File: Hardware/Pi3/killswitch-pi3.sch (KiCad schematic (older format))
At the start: 32 parts, among them J1 PWR_IN, J2 REMOTE, J3 PI, J4 Conn_01x02, J5 Conn_01x02, Q1 Q_PMOS_GSD, SW1 SW_Push, U1 ATTINY84-20SSU, U2 TSDP341xx, U3 AZ1117-3.3, U4 TXB0108DQSR

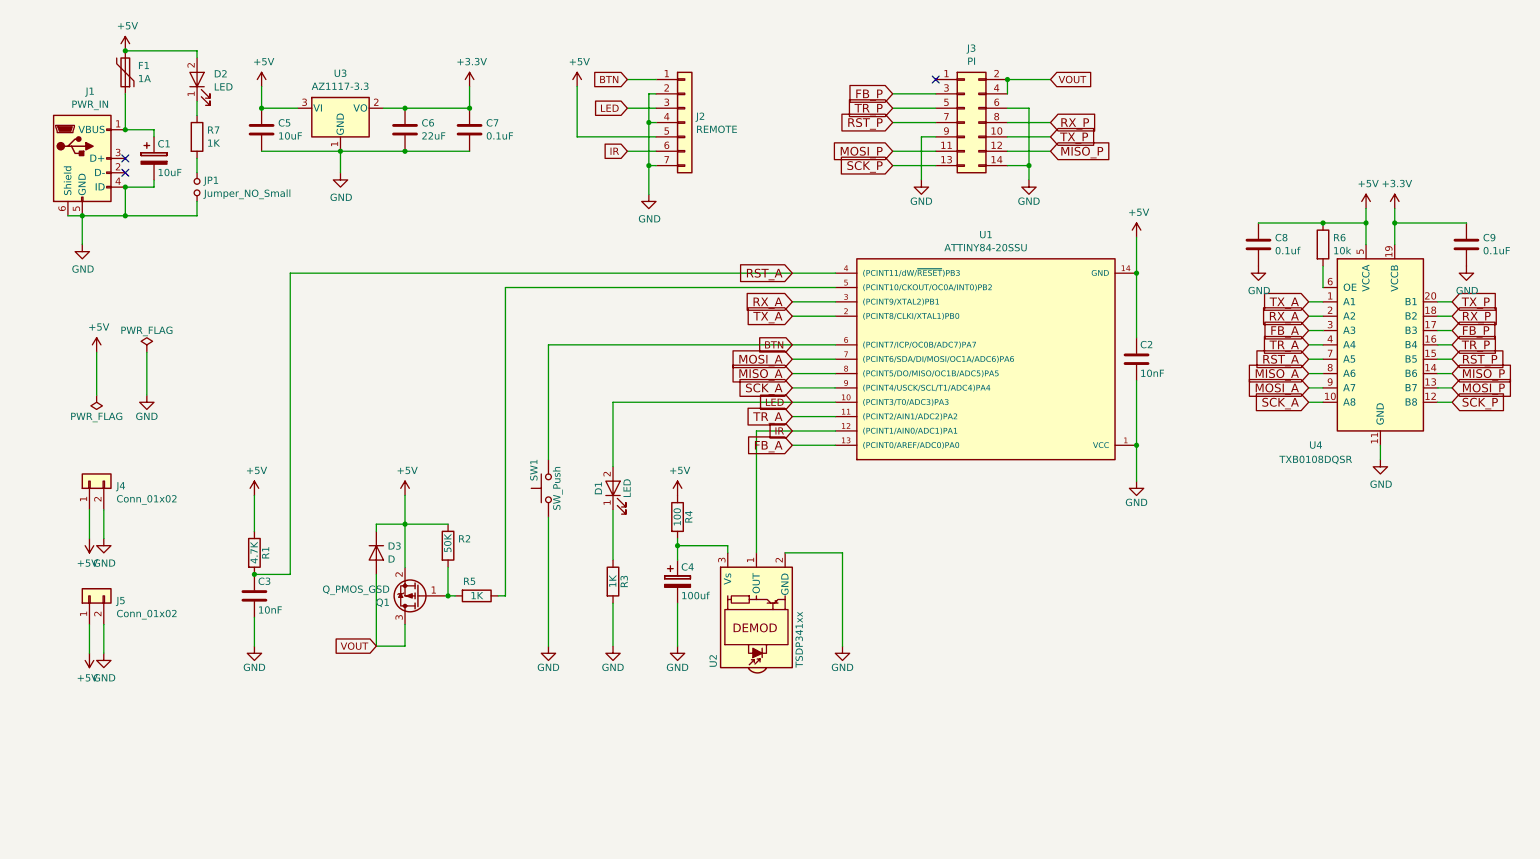
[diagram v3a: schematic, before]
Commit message: Clean up schematic/remove level shifter
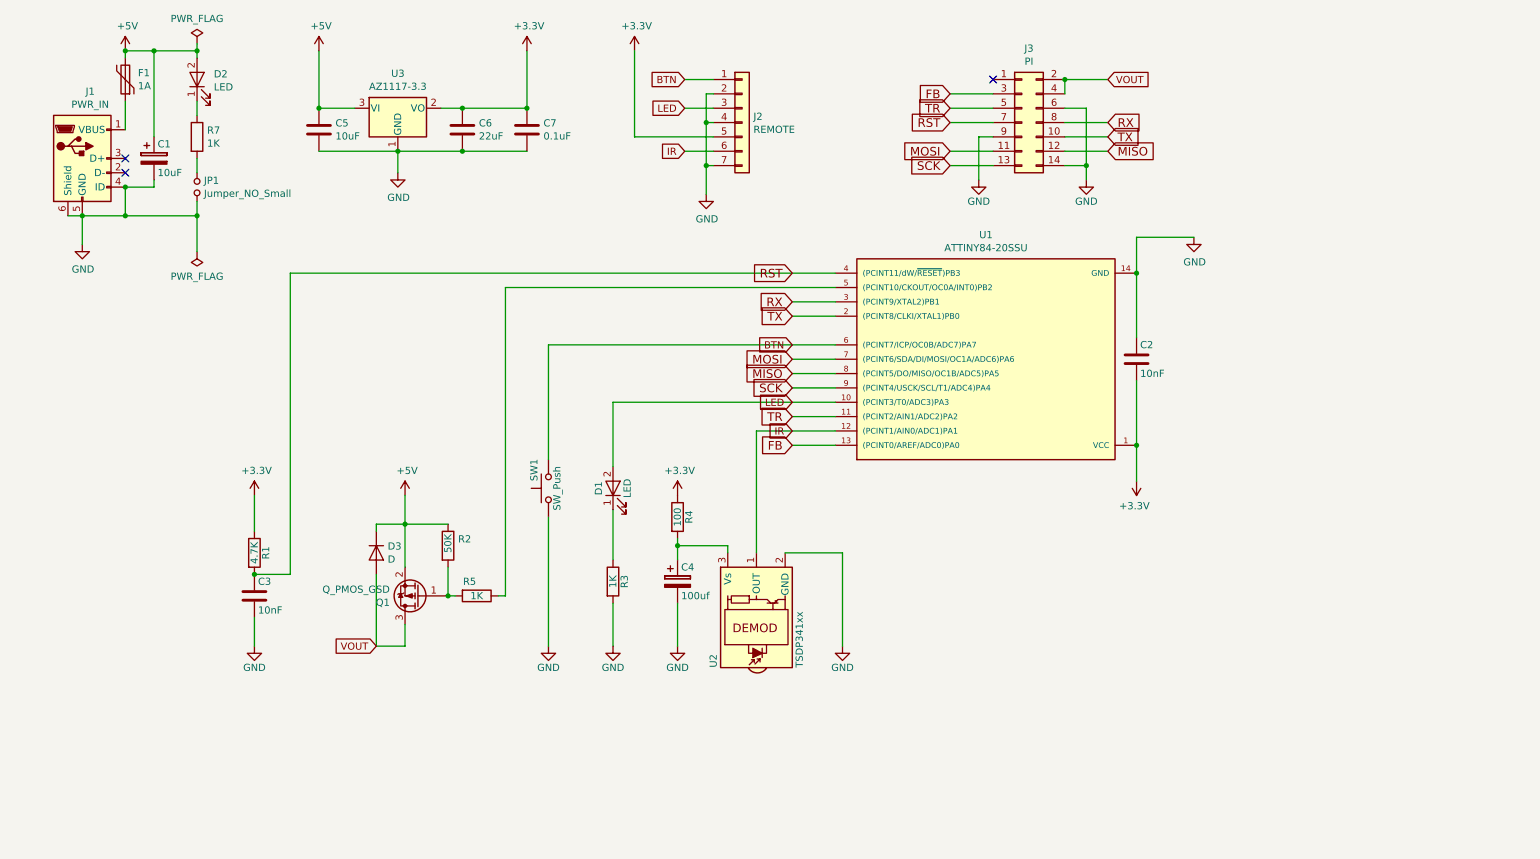
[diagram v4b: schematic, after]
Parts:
- removed C8: 0.1uf, Capacitors_SMD:C_0603_HandSoldering, symbol device:C
- removed C9: 0.1uF, Capacitors_SMD:C_0603_HandSoldering, symbol device:C
- removed J4: Conn_01x02, Connectors_JST:JST_XH_B02B-XH-A_02x2.50mm_Straight, symbol conn:Conn_01x02
- removed J5: Conn_01x02, Pin_Headers:Pin_Header_Straight_1x02_Pitch2.54mm, symbol conn:Conn_01x02
- removed R6: 10k, Resistors_SMD:R_0603_HandSoldering, symbol device:R
- removed U4: TXB0108DQSR, Housings_SON:USON-20_2x4mm_Pitch0.4mm, symbol texas:TXB0108DQSR
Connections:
- net FB_P is gone; now on net FB: J3.3 (Pin_3)
- net MISO_P is gone; now on net MISO: J3.12 (Pin_12)
- net MOSI_P is gone; now on net MOSI: J3.11 (Pin_11)
- net RST_P is gone; now on net RST: J3.7 (Pin_7)
- net RX_P is gone; now on net RX: J3.8 (Pin_8)
- net SCK_P is gone; now on net SCK: J3.13 (Pin_13)
- net TR_P is gone; now on net TR: J3.5 (Pin_5)
- net TX_P is gone; now on net TX: J3.10 (Pin_10)
- net +3V3: now also C2.2, J2.5 (Pin_5), R1.1, R4.1, U1.1 (VCC)
- net +5V: now also C1.1; no longer C2.1, J2.5 (Pin_5), R1.1, R4.1, U1.14 (GND)
- net GND: now also C2.1, U1.14 (GND); no longer C2.2, U1.1 (VCC)
- net at F1.1, J1.1 (VBUS): no longer C1.1
- net FB_A renamed FB
- net MISO_A renamed MISO
- net MOSI_A renamed MOSI
- net RST_A renamed RST
- net RX_A renamed RX
- net SCK_A renamed SCK
- net TR_A renamed TR
- net TX_A renamed TX
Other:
- moved on the sheet: C5, C6, C7, F1, J2, J3, U3

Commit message: changed to ATTiny1634
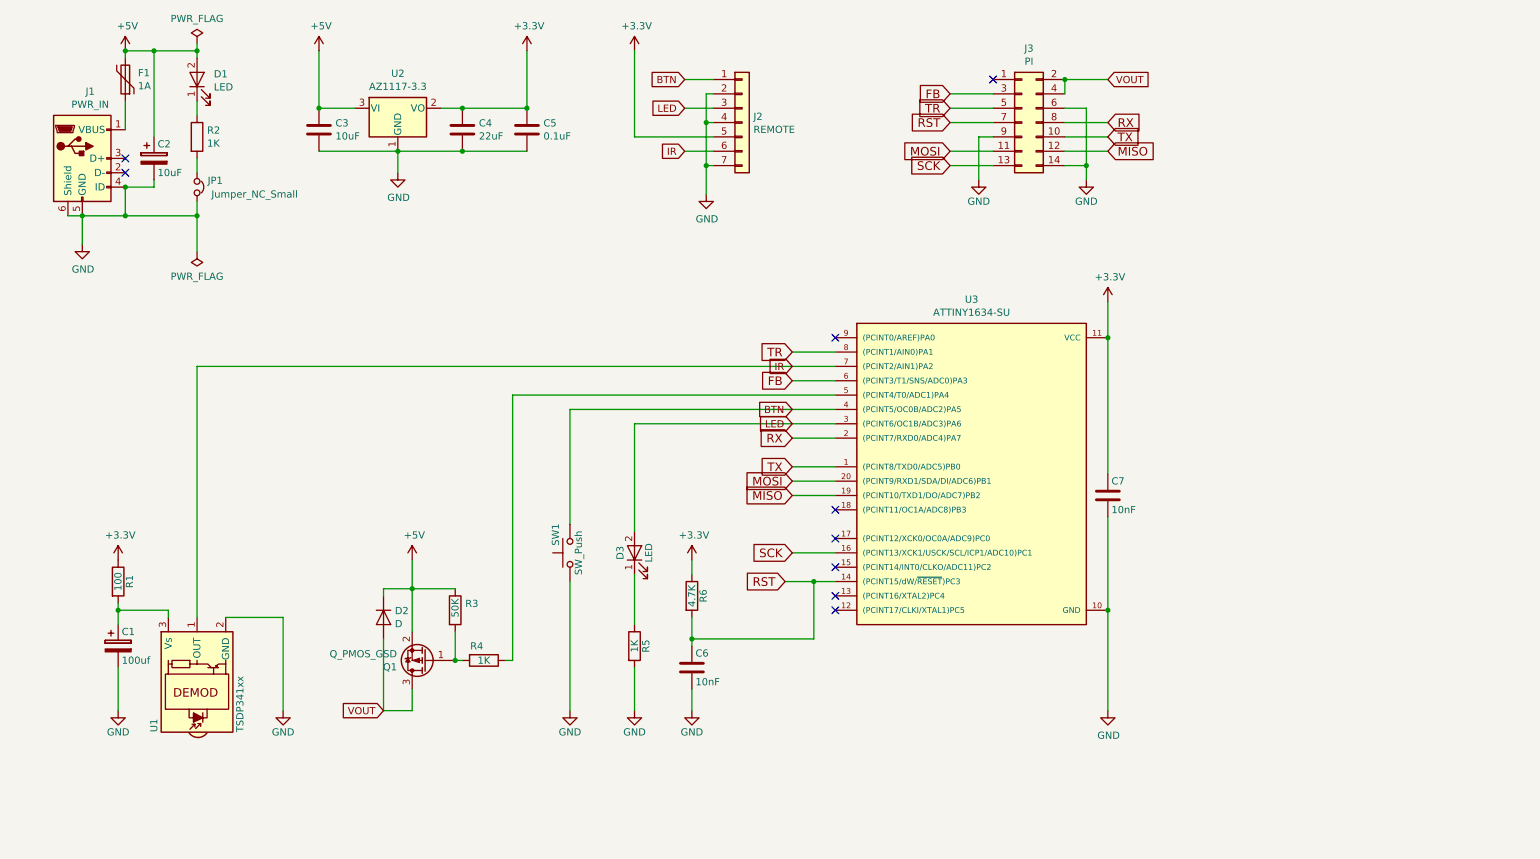
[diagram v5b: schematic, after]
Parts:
- removed JP1: Jumper_NO_Small, Jumper:SolderJumper-2_P1.3mm_Bridged2Bar_Pad1.0x1.5mm, symbol device:Jumper_NO_Small
- removed U1: ATTINY84-20SSU, Housings_SOIC:SOIC-14_3.9x8.7mm_Pitch1.27mm, symbol atmel:ATTINY84-20SSU
- added JP1: Jumper_NC_Small, Jumper:SolderJumper-2_P1.3mm_Bridged_Pad1.0x1.5mm, symbol device:Jumper_NC_Small
- added U3: ATTINY1634-SU, Housings_SOIC:SOIC-20W_7.5x12.8mm_Pitch1.27mm, symbol atmel:ATTINY1634-SU
- renumbered C4 to C1, C1 to C2, C5 to C3, C6 to C4, C7 to C5, C3 to C6, C2 to C7, D2 to D1, D3 to D2, D1 to D3, R4 to R1, R7 to R2, R2 to R3, R5 to R4, R3 to R5, R1 to R6, U2 to U1, U3 to U2
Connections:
- net +3V3: now also C7.1, U3.11 (VCC); no longer C7.2
- net BTN: now also U3.4 ((PCINT5/OC0B/ADC2)PA5)
- net FB: now also U3.6 ((PCINT3/T1/SNS/ADC0)PA3)
- net GND: now also C7.2, JP1.2, U3.10 (GND); no longer C7.1
- net IR: now also U3.7 ((PCINT2/AIN1)PA2)
- net LED: now also U3.3 ((PCINT6/OC1B/ADC3)PA6)
- net MISO: now also U3.19 ((PCINT10/TXD1/DO/ADC7)PB2)
- net MOSI: now also U3.20 ((PCINT9/RXD1/SDA/DI/ADC6)PB1)
- net RST: now also U3.14 ((PCINT15/dW/~RESET~)PC3)
- net RX: now also U3.2 ((PCINT7/RXD0/ADC4)PA7)
- net SCK: now also U3.16 ((PCINT13/XCK1/USCK/SCL/ICP1/ADC10)PC1)
- net TR: now also U3.8 ((PCINT1/AIN0)PA1)
- net TX: now also U3.1 ((PCINT8/TXD0/ADC5)PB0)
- net at R4.1: now also U3.5 ((PCINT4/T0/ADC1)PA4)
- net at R2.2: now also JP1.1
- no-connect marks 3 -> 9
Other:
- moved on the sheet: C1, C6, C7, D2, D3, Q1, R1, R3, R4, R5, R6, SW1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

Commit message: new schematic/pcb for 1634
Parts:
- D1: value LED -> LED_PWR_IN
- D2: value D -> PWR_ICSP
- D3: value LED -> LED_STATUS
- JP1: value Jumper_NC_Small -> JPR_PWR_IN
- R5: value 1K -> 333
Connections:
- net +3V3: no longer J2.5 (Pin_5)
- net BTN: now also U3.3 ((PCINT6/OC1B/ADC3)PA6); no longer U3.4 ((PCINT5/OC0B/ADC2)PA5)
- net LED: now also U3.4 ((PCINT5/OC0B/ADC2)PA5); no longer U3.3 ((PCINT6/OC1B/ADC3)PA6)
- net IR+: now reaches C1.1, R1.2, U1.3 (Vs)
- net IR+: now also J2.5 (Pin_5)
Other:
- moved on the sheet: C1, C2, C3, C4, C5, C6, C7, D1, D2, D3, F1, J2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
